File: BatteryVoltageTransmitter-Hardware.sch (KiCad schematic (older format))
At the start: 4 parts, among them U1 MSP_EXP432P401R_Launchpad_Shi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, U2 Raspberry_Pi

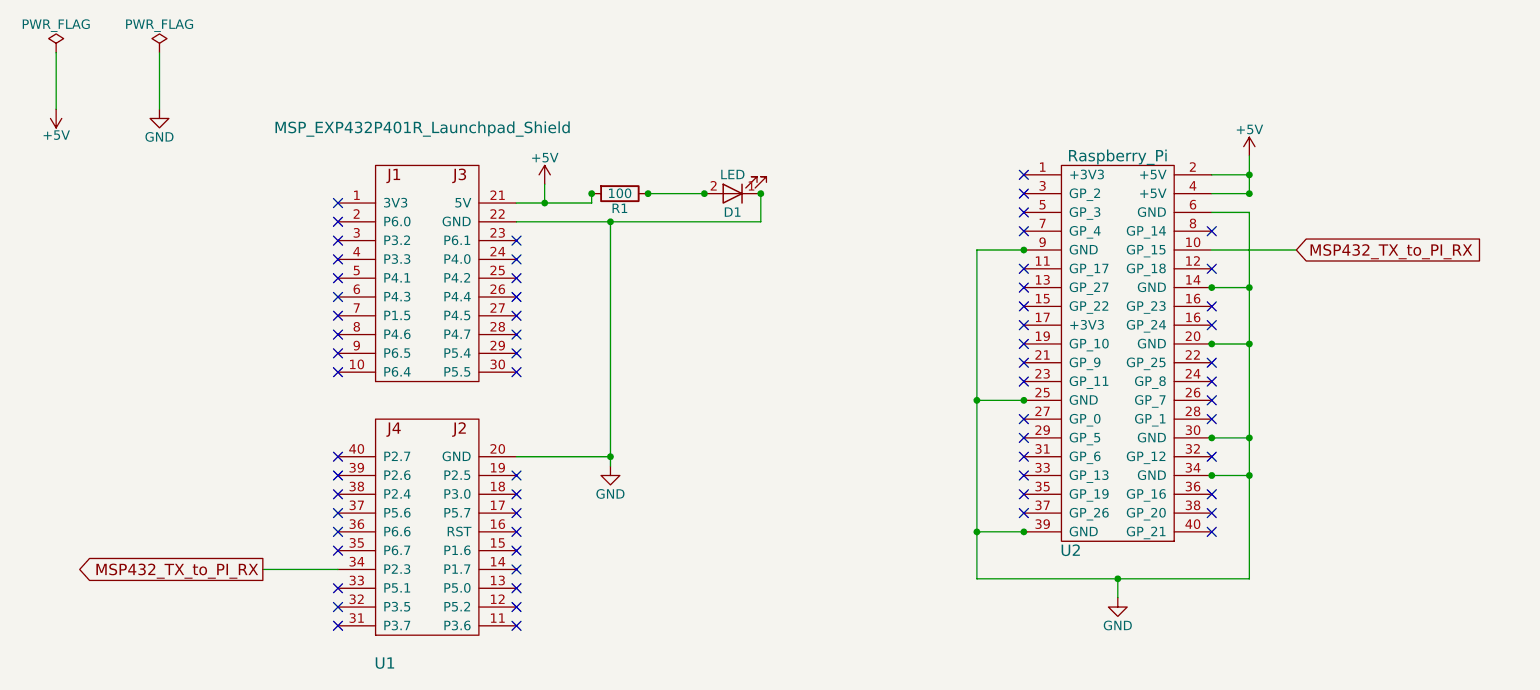
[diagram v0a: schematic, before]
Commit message: Added MRDT Logo and Cleaned Schematic
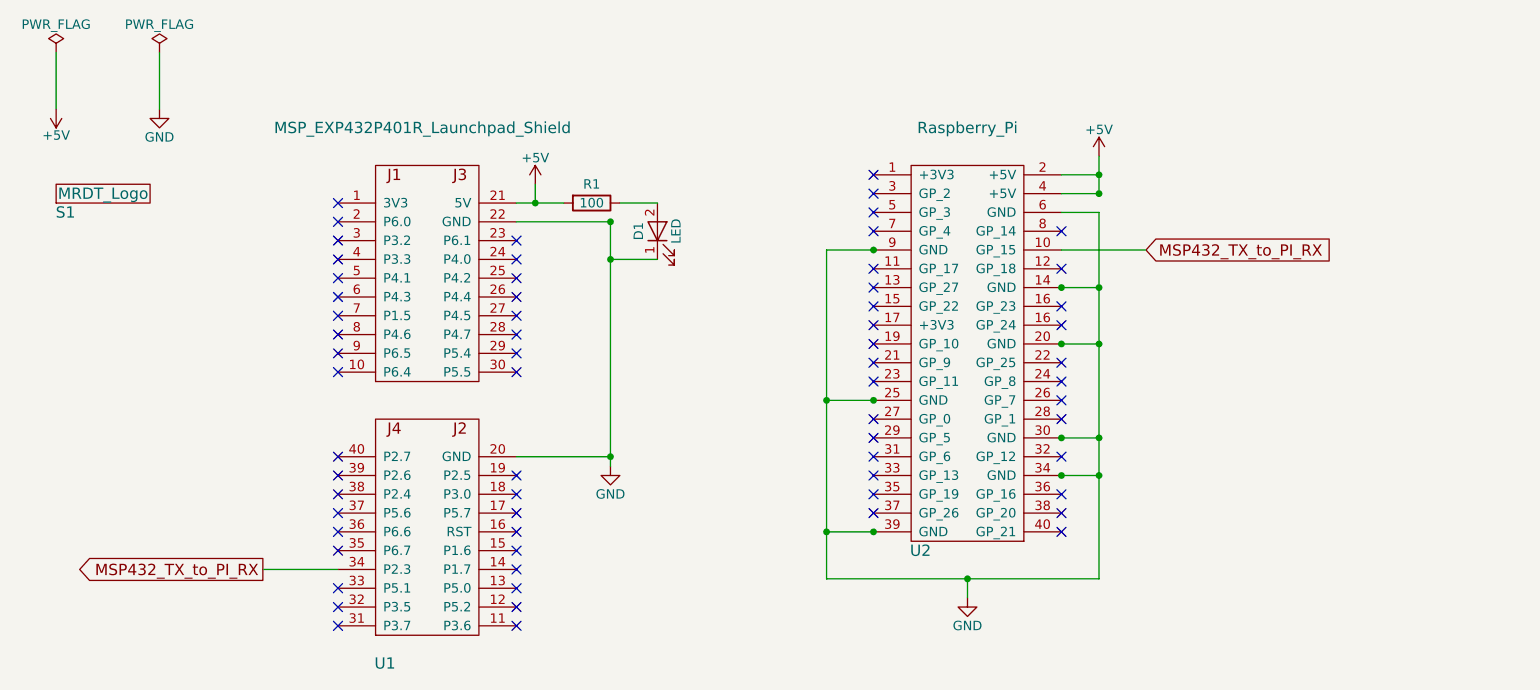
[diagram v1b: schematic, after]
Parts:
- added S1: MRDT_Logo, MRDT-Silkscreens:MRDT_Logo_7.5mm, symbol MRDT_Logo
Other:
- moved on the sheet: D1, R1, U2

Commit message: Logos updated
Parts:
- removed S1: MRDT_Logo, MRDT-Silkscreens:MRDT_Logo_7.5mm, symbol MRDT_Logo
- added S1: Logo_or_Signature, MRDT-Silkscreens:MRDT_Logo_7.5mm, symbol Logo_or_Signature
- added S2: Logo_or_Signature, MRDT-Silkscreens:Atlas_Logo_28.6mmX37.3mm, symbol Logo_or_Signature
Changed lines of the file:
@@
 Connection ~ 4000 2400
 $Comp
-L MRDT_Logo S1
-U 1 1 5AA4D166
-P 1050 2100
-F 0 "S1" H 1100 2050 60  0000 C CNN
-F 1 "MRDT_Logo" H 1300 2150 60  0000 C CNN
-F 2 "MRDT-Silkscreens:MRDT_Logo_7.5mm" H 1050 2100 60  0001 C CNN
-F 3 "" H 1050 2100 60  0001 C CNN
-	1    1050 2100
+L Logo_or_Signature S1
+U 1 1 5AA585EB
+P 900 2150
+F 0 "S1" H 950 2100 60  0000 C CNN
+F 1 "Logo_or_Signature" H 1350 2200 60  0000 C CNN
+F 2 "MRDT-Silkscreens:MRDT_Logo_7.5mm" H 900 2150 60  0001 C CNN
+F 3 "" H 900 2150 60  0001 C CNN
+	1    900  2150
 	1    0    0    -1
 $EndComp
+$Comp
+L Logo_or_Signature S2
+U 1 1 5AA5861E
+P 900 2350
+F 0 "S2" H 950 2300 60  0000 C CNN
+F 1 "Logo_or_Signature" H 1350 2400 60  0000 C CNN
+F 2 "MRDT-Silkscreens:Atlas_Logo_28.6mmX37.3mm" H 900 2350 60  0001 C CNN
+F 3 "" H 900 2350 60  0001 C CNN
+	1    900  2350
+	1    0    0    -1
+$EndComp
